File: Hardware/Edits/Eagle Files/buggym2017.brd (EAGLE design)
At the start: 88.9 x 81.3 mm, 6 parts, among them IC1-NOR 4001N, IC2-OR 4075N, IC3 BCC, IC4 L293E

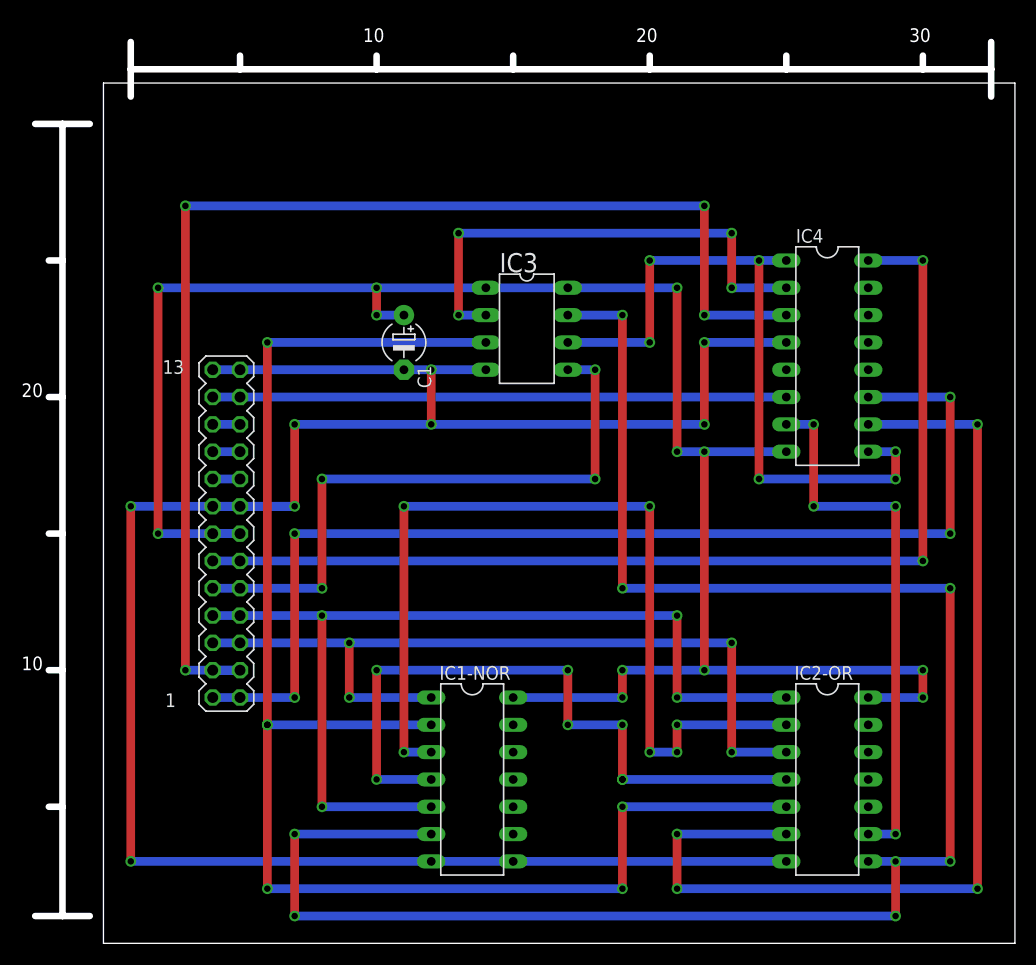
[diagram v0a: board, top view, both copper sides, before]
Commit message: Rerouted ground and the left motor signal Ground went around the header in a column that is not actually present on the board. Fixed Moved 3 pre-placed wires, so that the left motor signal wire does not have to go under the H-bridge. All changes are in diameter 0.016 (thin) red wire
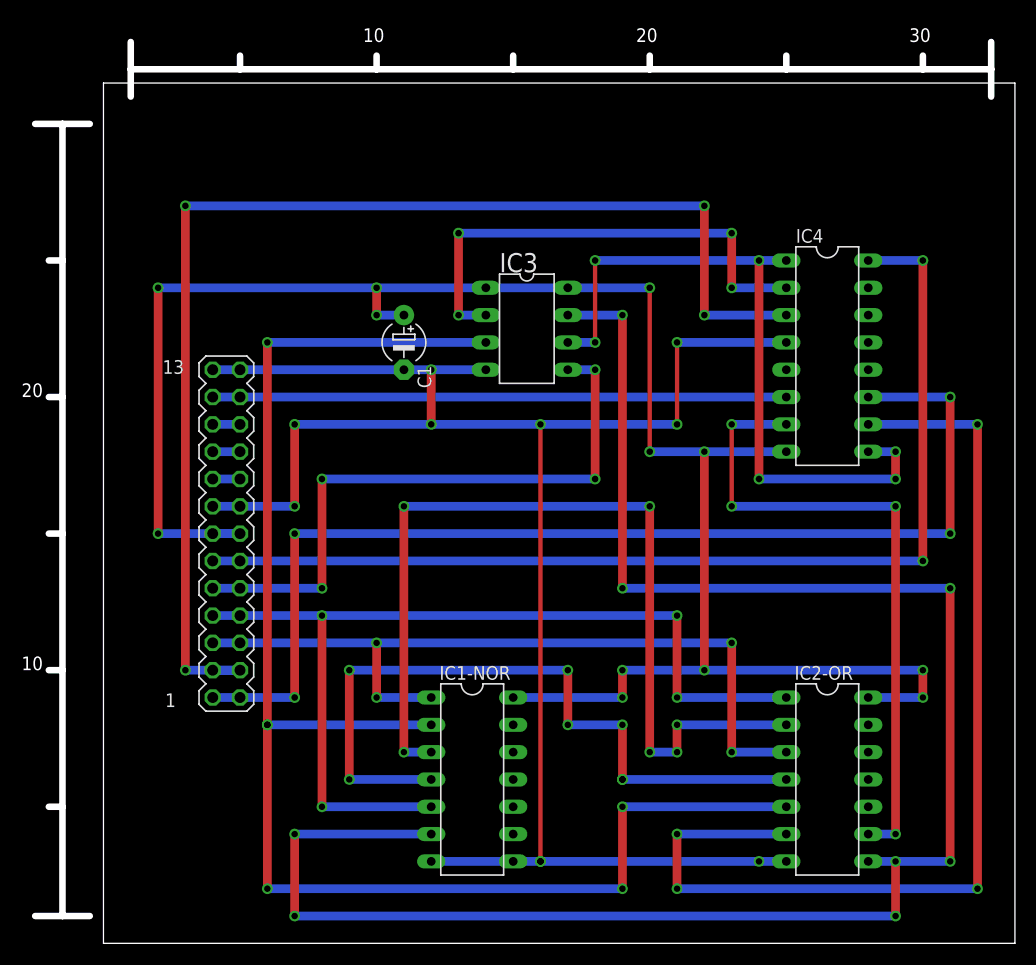
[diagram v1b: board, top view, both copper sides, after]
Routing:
- net GND: track 203.2 -> 167.6 mm, vias 8 -> 10
- net LM: track 50.8 -> 61.0 mm
- net LINK_2: track 63.5 -> 68.6 mm
- net R_EYE: track 73.7 -> 71.1 mm
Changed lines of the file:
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@@
 <?xml version="1.0" encoding="utf-8"?>
 <!DOCTYPE eagle SYSTEM "eagle.dtd">
-<eagle version="7.7.0">
+<eagle version="8.0.1">
 <drawing>
 <settings>
@@
 <text x="65.405" y="42.545" size="1.778" layer="19">X</text>
 <text x="29.845" y="42.545" size="1.778" layer="19">X</text>
-<text x="65.405" y="45.085" size="1.778" layer="19">X</text>
+<text x="62.865" y="45.085" size="1.778" layer="19">X</text>
 <text x="83.185" y="45.085" size="1.778" layer="19">X</text>
 <text x="83.185" y="47.625" size="1.778" layer="19">X</text>
 <text x="83.185" y="50.165" size="1.778" layer="19">X</text>
 <text x="83.185" y="62.865" size="1.778" layer="19">X</text>
-<text x="73.025" y="47.625" size="1.778" layer="19">X</text>
+<text x="70.485" y="47.625" size="1.778" layer="19">X</text>
 <text x="29.845" y="47.625" size="1.778" layer="19">X</text>
 <text x="55.245" y="52.705" size="1.778" layer="19">X</text>
@@
 <text x="55.245" y="57.785" size="1.778" layer="19">X</text>
 <text x="70.485" y="60.325" size="1.778" layer="19">X</text>
-<text x="67.945" y="57.785" size="1.778" layer="19">X</text>
-<text x="67.945" y="55.245" size="1.778" layer="19">X</text>
+<text x="65.405" y="57.785" size="1.778" layer="19">X</text>
+<text x="65.405" y="55.245" size="1.778" layer="19">X</text>
 <text x="45.085" y="57.785" size="1.778" layer="19">X</text>
 <text x="83.185" y="60.325" size="1.778" layer="19">X</text>
 <text x="83.185" y="57.785" size="1.778" layer="19">X</text>
-<text x="67.945" y="52.705" size="1.778" layer="19">X</text>
+<text x="65.405" y="52.705" size="1.778" layer="19">X</text>
 <text x="83.185" y="22.225" size="1.778" layer="19">X</text>
 <text x="83.185" y="19.685" size="1.778" layer="19">X</text>
@@
 <contactref element="IC4" pad="9"/>
 <contactref element="IC4" pad="1"/>
-<wire x1="58.42" y1="55.88" x2="66.04" y2="55.88" width="0.8128" layer="16"/>
-<via x="66.04" y="55.88" extent="1-16" drill="0.6096" shape="square"/>
-<wire x1="66.04" y1="55.88" x2="66.04" y2="63.5" width="0.8128" layer="1"/>
-<via x="66.04" y="63.5" extent="1-16" drill="0.6096" shape="square"/>
-<wire x1="66.04" y1="63.5" x2="76.2" y2="63.5" width="0.8128" layer="16"/>
+<wire x1="58.42" y1="55.88" x2="60.96" y2="55.88" width="0.8128" layer="16"/>
+<via x="60.96" y="55.88" extent="1-16" drill="0.6096" shape="square"/>
+<wire x1="60.96" y1="55.88" x2="60.96" y2="63.5" width="0.4064" layer="1"/>
+<via x="60.96" y="63.5" extent="1-16" drill="0.6096" shape="square"/>
+<wire x1="60.96" y1="63.5" x2="76.2" y2="63.5" width="0.8128" layer="16"/>
 <wire x1="76.2" y1="63.5" x2="78.74" y2="63.5" width="0.8128" layer="16"/>
 <wire x1="86.36" y1="45.72" x2="88.9" y2="45.72" width="0.8128" layer="16"/>
@@
 <wire x1="40.64" y1="58.42" x2="40.64" y2="60.96" width="0.8128" layer="1"/>
 <wire x1="78.74" y1="45.72" x2="71.12" y2="45.72" width="0.8128" layer="16"/>
-<via x="68.58" y="45.72" extent="1-16" drill="0.6096" shape="square"/>
-<wire x1="71.12" y1="45.72" x2="68.58" y2="45.72" width="0.8128" layer="16"/>
-<wire x1="68.58" y1="45.72" x2="68.58" y2="60.96" width="0.8128" layer="1"/>
-<via x="68.58" y="60.96" extent="1-16" drill="0.6096" shape="square"/>
-<wire x1="68.58" y1="60.96" x2="58.42" y2="60.96" width="0.8128" layer="16"/>
+<via x="66.04" y="45.72" extent="1-16" drill="0.6096" shape="square"/>
+<wire x1="71.12" y1="45.72" x2="66.04" y2="45.72" width="0.8128" layer="16"/>
+<wire x1="66.04" y1="45.72" x2="66.04" y2="60.96" width="0.4064" layer="1"/>
+<via x="66.04" y="60.96" extent="1-16" drill="0.6096" shape="square"/>
+<wire x1="66.04" y1="60.96" x2="58.42" y2="60.96" width="0.8128" layer="16"/>
 <via x="40.64" y="60.96" extent="1-16" drill="0.6096" shape="square"/>
 <contactref element="IC1-NOR" pad="14"/>
@@
 <wire x1="43.18" y1="53.34" x2="45.72" y2="53.34" width="0.8128" layer="16"/>
 <wire x1="45.72" y1="53.34" x2="50.8" y2="53.34" width="0.8128" layer="16"/>
-<wire x1="78.74" y1="55.88" x2="71.12" y2="55.88" width="0.8128" layer="16"/>
-<via x="71.12" y="55.88" extent="1-16" drill="0.6096" shape="square"/>
-<wire x1="71.12" y1="55.88" x2="71.12" y2="48.26" width="0.8128" layer="1"/>
-<via x="71.12" y="48.26" extent="1-16" drill="0.6096" shape="square"/>
-<wire x1="71.12" y1="48.26" x2="45.72" y2="48.26" width="0.8128" layer="16"/>
+<wire x1="78.74" y1="55.88" x2="68.58" y2="55.88" width="0.8128" layer="16"/>
+<via x="68.58" y="55.88" extent="1-16" drill="0.6096" shape="square"/>
+<wire x1="68.58" y1="55.88" x2="68.58" y2="48.26" width="0.4064" layer="1"/>
+<via x="68.58" y="48.26" extent="1-16" drill="0.6096" shape="square"/>
+<wire x1="68.58" y1="48.26" x2="55.88" y2="48.26" width="0.8128" layer="16"/>
 <via x="45.72" y="48.26" extent="1-16" drill="0.6096" shape="square"/>
+<wire x1="55.88" y1="48.26" x2="45.72" y2="48.26" width="0.8128" layer="16"/>
 <wire x1="45.72" y1="48.26" x2="45.72" y2="53.34" width="0.8128" layer="1"/>
 <contactref element="BUGGY_CON" pad="8"/>
@@
 <contactref element="IC2-OR" pad="7"/>
 <wire x1="27.94" y1="40.64" x2="33.02" y2="40.64" width="0.8128" layer="16"/>
-<wire x1="33.02" y1="40.64" x2="17.78" y2="40.64" width="0.8128" layer="16"/>
-<via x="17.78" y="40.64" extent="1-16" drill="0.6" shape="square"/>
-<wire x1="17.78" y1="40.64" x2="17.78" y2="7.62" width="0.8128" layer="1"/>
-<via x="17.78" y="7.62" extent="1-16" drill="0.6" shape="square"/>
-<wire x1="17.78" y1="7.62" x2="45.72" y2="7.62" width="0.8128" layer="16"/>
-<wire x1="45.72" y1="7.62" x2="78.74" y2="7.62" width="0.8128" layer="16"/>
+<wire x1="45.72" y1="7.62" x2="55.88" y2="7.62" width="0.8128" layer="16"/>
+<wire x1="55.88" y1="7.62" x2="76.2" y2="7.62" width="0.8128" layer="16"/>
+<wire x1="76.2" y1="7.62" x2="78.74" y2="7.62" width="0.8128" layer="16"/>
+<via x="76.2" y="7.62" extent="1-16" drill="0.6" shape="square"/>
+<via x="55.88" y="7.62" extent="1-16" drill="0.6" shape="square"/>
+<via x="55.88" y="7.62" extent="1-16" drill="0.6" shape="square"/>
+<wire x1="55.88" y1="7.62" x2="55.88" y2="48.26" width="0.4064" layer="1"/>
+<via x="55.88" y="48.26" extent="1-16" drill="0.6" shape="square"/>
 </signal>
 <signal name="N$2">
@@
 <contactref element="BUGGY_CON" pad="3"/>
 <contactref element="IC2-OR" pad="3"/>
-<wire x1="38.1" y1="27.94" x2="27.94" y2="27.94" width="0.8128" layer="16"/>
-<via x="38.1" y="27.94" extent="1-16" drill="0.6" shape="square"/>
-<wire x1="38.1" y1="27.94" x2="38.1" y2="22.86" width="0.8128" layer="1"/>
-<via x="38.1" y="22.86" extent="1-16" drill="0.6" shape="square"/>
-<wire x1="38.1" y1="22.86" x2="45.72" y2="22.86" width="0.8128" layer="16"/>
+<wire x1="40.64" y1="27.94" x2="27.94" y2="27.94" width="0.8128" layer="16"/>
+<via x="40.64" y="27.94" extent="1-16" drill="0.6" shape="square"/>
+<wire x1="40.64" y1="27.94" x2="40.64" y2="22.86" width="0.8128" layer="1"/>
+<via x="40.64" y="22.86" extent="1-16" drill="0.6" shape="square"/>
+<wire x1="40.64" y1="22.86" x2="45.72" y2="22.86" width="0.8128" layer="16"/>
 <wire x1="78.74" y1="17.78" x2="73.66" y2="17.78" width="0.8128" layer="16"/>
 <via x="73.66" y="17.78" extent="1-16" drill="0.6" shape="square"/>
 <wire x1="73.66" y1="17.78" x2="73.66" y2="27.94" width="0.8128" layer="1"/>
 <via x="73.66" y="27.94" extent="1-16" drill="0.6" shape="square"/>
-<wire x1="73.66" y1="27.94" x2="38.1" y2="27.94" width="0.8128" layer="16"/>
+<wire x1="73.66" y1="27.94" x2="40.64" y2="27.94" width="0.8128" layer="16"/>
 </signal>
 <signal name="L_EYE">
@@
 <contactref element="IC1-NOR" pad="4"/>
 <contactref element="IC2-OR" pad="4"/>
-<wire x1="45.72" y1="15.24" x2="40.64" y2="15.24" width="0.8128" layer="16"/>
-<via x="40.64" y="15.24" extent="1-16" drill="0.6" shape="square"/>
-<wire x1="40.64" y1="15.24" x2="40.64" y2="25.4" width="0.8128" layer="1"/>
-<via x="40.64" y="25.4" extent="1-16" drill="0.6" shape="square"/>
-<wire x1="40.64" y1="25.4" x2="58.42" y2="25.4" width="0.8128" layer="16"/>
+<wire x1="45.72" y1="15.24" x2="38.1" y2="15.24" width="0.8128" layer="16"/>
+<via x="38.1" y="15.24" extent="1-16" drill="0.6" shape="square"/>
+<wire x1="38.1" y1="15.24" x2="38.1" y2="25.4" width="0.8128" layer="1"/>
+<via x="38.1" y="25.4" extent="1-16" drill="0.6" shape="square"/>
+<wire x1="38.1" y1="25.4" x2="58.42" y2="25.4" width="0.8128" layer="16"/>
 <via x="58.42" y="25.4" extent="1-16" drill="0.6" shape="square"/>
 <wire x1="58.42" y1="25.4" x2="58.42" y2="20.32" width="0.8128" layer="1"/>
@@
 <wire x1="88.9" y1="10.16" x2="88.9" y2="40.64" width="0.8128" layer="1"/>
 <via x="88.9" y="40.64" extent="1-16" drill="0.6" shape="square"/>
-<wire x1="88.9" y1="40.64" x2="81.28" y2="40.64" width="0.8128" layer="16"/>
-<via x="81.28" y="40.64" extent="1-16" drill="0.6" shape="square"/>
-<wire x1="81.28" y1="40.64" x2="81.28" y2="48.26" width="0.8128" layer="1"/>
-<via x="81.28" y="48.26" extent="1-16" drill="0.6" shape="square"/>
-<wire x1="81.28" y1="48.26" x2="78.74" y2="48.26" width="0.8128" layer="16"/>
+<wire x1="88.9" y1="40.64" x2="73.66" y2="40.64" width="0.8128" layer="16"/>
+<via x="73.66" y="40.64" extent="1-16" drill="0.6" shape="square"/>
+<wire x1="73.66" y1="40.64" x2="73.66" y2="48.26" width="0.4064" layer="1"/>
+<via x="73.66" y="48.26" extent="1-16" drill="0.6" shape="square"/>
+<wire x1="73.66" y1="48.26" x2="78.74" y2="48.26" width="0.8128" layer="16"/>
 </signal>
 <signal name="RM">

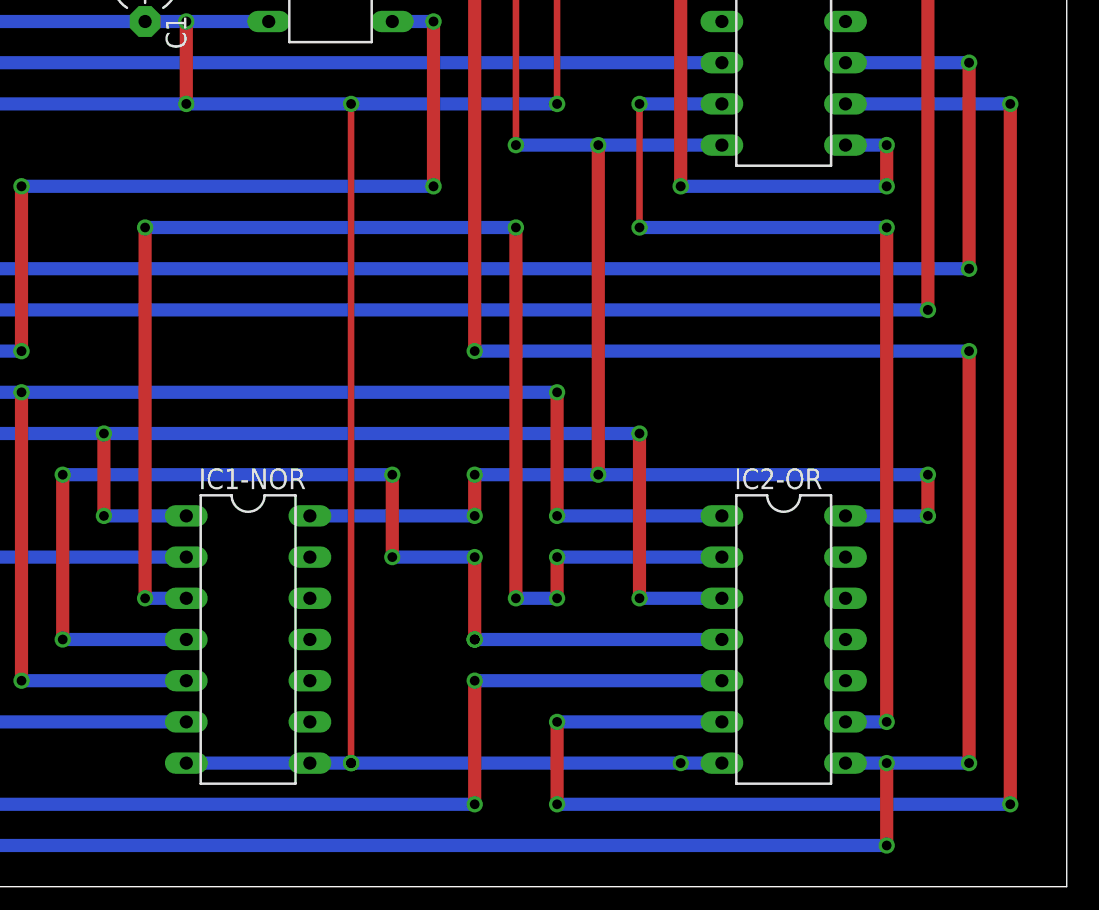
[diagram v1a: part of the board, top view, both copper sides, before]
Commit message: Work done in Hardware Lab 5
Finished schematic and new Arduino Sketch, blink without delay
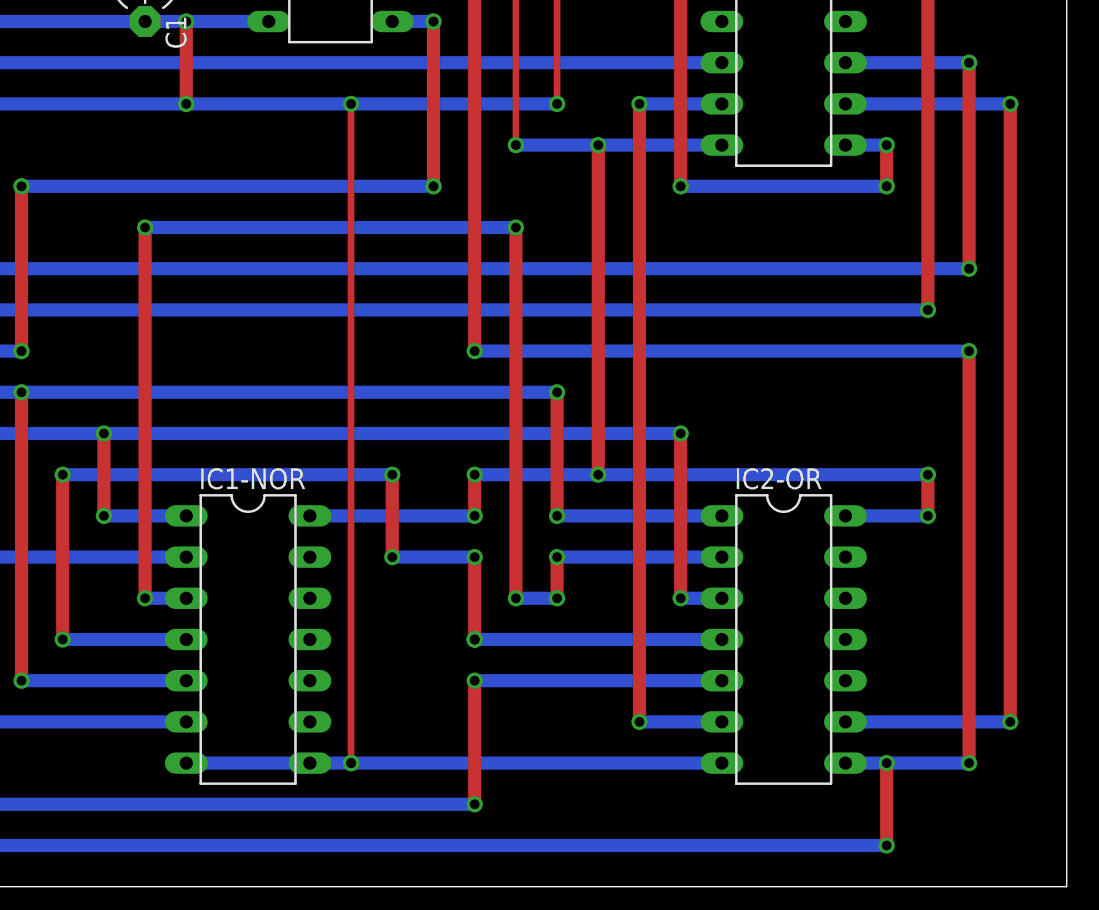
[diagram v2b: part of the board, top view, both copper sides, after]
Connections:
- net LM: now also IC4.10; no longer IC4.7
- net RM: now also IC4.7; no longer IC4.10
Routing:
- net RM: track 96.5 -> 48.3 mm, vias 4 -> 2
- net LM: track 61.0 -> 58.4 mm, vias 4 -> 2
- net GND: vias 10 -> 9
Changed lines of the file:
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@@
 <?xml version="1.0" encoding="utf-8"?>
 <!DOCTYPE eagle SYSTEM "eagle.dtd">
-<eagle version="8.0.1">
+<eagle version="7.7.0">
 <drawing>
 <settings>
@@
 <wire x1="27.94" y1="40.64" x2="33.02" y2="40.64" width="0.8128" layer="16"/>
 <wire x1="45.72" y1="7.62" x2="55.88" y2="7.62" width="0.8128" layer="16"/>
-<wire x1="55.88" y1="7.62" x2="76.2" y2="7.62" width="0.8128" layer="16"/>
-<wire x1="76.2" y1="7.62" x2="78.74" y2="7.62" width="0.8128" layer="16"/>
-<via x="76.2" y="7.62" extent="1-16" drill="0.6" shape="square"/>
 <via x="55.88" y="7.62" extent="1-16" drill="0.6" shape="square"/>
 <via x="55.88" y="7.62" extent="1-16" drill="0.6" shape="square"/>
 <wire x1="55.88" y1="7.62" x2="55.88" y2="48.26" width="0.4064" layer="1"/>
 <via x="55.88" y="48.26" extent="1-16" drill="0.6" shape="square"/>
+<wire x1="55.88" y1="7.62" x2="78.74" y2="7.62" width="0.8128" layer="16"/>
 </signal>
 <signal name="N$2">
@@
 <via x="40.64" y="22.86" extent="1-16" drill="0.6" shape="square"/>
 <wire x1="40.64" y1="22.86" x2="45.72" y2="22.86" width="0.8128" layer="16"/>
-<wire x1="78.74" y1="17.78" x2="73.66" y2="17.78" width="0.8128" layer="16"/>
-<via x="73.66" y="17.78" extent="1-16" drill="0.6" shape="square"/>
-<wire x1="73.66" y1="17.78" x2="73.66" y2="27.94" width="0.8128" layer="1"/>
-<via x="73.66" y="27.94" extent="1-16" drill="0.6" shape="square"/>
-<wire x1="73.66" y1="27.94" x2="40.64" y2="27.94" width="0.8128" layer="16"/>
+<wire x1="78.74" y1="17.78" x2="76.2" y2="17.78" width="0.8128" layer="16"/>
+<via x="76.2" y="17.78" extent="1-16" drill="0.6" shape="square"/>
+<wire x1="76.2" y1="17.78" x2="76.2" y2="27.94" width="0.8128" layer="1"/>
+<via x="76.2" y="27.94" extent="1-16" drill="0.6" shape="square"/>
+<wire x1="76.2" y1="27.94" x2="40.64" y2="27.94" width="0.8128" layer="16"/>
 </signal>
 <signal name="L_EYE">
@@
 <signal name="LM">
 <contactref element="IC2-OR" pad="9"/>
+<contactref element="IC4" pad="10"/>
+<wire x1="86.36" y1="10.16" x2="96.52" y2="10.16" width="0.8128" layer="16"/>
+<via x="96.52" y="10.16" extent="1-16" drill="0.6" shape="square"/>
+<wire x1="96.52" y1="10.16" x2="96.52" y2="48.26" width="0.8128" layer="1"/>
+<via x="96.52" y="48.26" extent="1-16" drill="0.6" shape="square"/>
+<wire x1="96.52" y1="48.26" x2="86.36" y2="48.26" width="0.8128" layer="16"/>
+</signal>
+<signal name="RM">
+<contactref element="IC2-OR" pad="6"/>
 <contactref element="IC4" pad="7"/>
-<wire x1="86.36" y1="10.16" x2="88.9" y2="10.16" width="0.8128" layer="16"/>
-<via x="88.9" y="10.16" extent="1-16" drill="0.6" shape="square"/>
-<wire x1="88.9" y1="10.16" x2="88.9" y2="40.64" width="0.8128" layer="1"/>
-<via x="88.9" y="40.64" extent="1-16" drill="0.6" shape="square"/>
-<wire x1="88.9" y1="40.64" x2="73.66" y2="40.64" width="0.8128" layer="16"/>
-<via x="73.66" y="40.64" extent="1-16" drill="0.6" shape="square"/>
-<wire x1="73.66" y1="40.64" x2="73.66" y2="48.26" width="0.4064" layer="1"/>
+<wire x1="78.74" y1="10.16" x2="73.66" y2="10.16" width="0.8128" layer="16"/>
+<via x="73.66" y="10.16" extent="1-16" drill="0.6" shape="square"/>
+<wire x1="73.66" y1="10.16" x2="73.66" y2="48.26" width="0.8128" layer="1"/>
 <via x="73.66" y="48.26" extent="1-16" drill="0.6" shape="square"/>
 <wire x1="73.66" y1="48.26" x2="78.74" y2="48.26" width="0.8128" layer="16"/>
 </signal>
-<signal name="RM">
-<contactref element="IC2-OR" pad="6"/>
-<contactref element="IC4" pad="10"/>
-<wire x1="78.74" y1="10.16" x2="68.58" y2="10.16" width="0.8128" layer="16"/>
-<via x="68.58" y="10.16" extent="1-16" drill="0.6" shape="square"/>
-<wire x1="68.58" y1="10.16" x2="68.58" y2="5.08" width="0.8128" layer="1"/>
-<via x="68.58" y="5.08" extent="1-16" drill="0.6" shape="square"/>
-<wire x1="68.58" y1="5.08" x2="96.52" y2="5.08" width="0.8128" layer="16"/>
-<via x="96.52" y="5.08" extent="1-16" drill="0.6" shape="square"/>
-<wire x1="96.52" y1="5.08" x2="96.52" y2="48.26" width="0.8128" layer="1"/>
-<via x="96.52" y="48.26" extent="1-16" drill="0.6" shape="square"/>
-<wire x1="96.52" y1="48.26" x2="86.36" y2="48.26" width="0.8128" layer="16"/>
-</signal>
 <signal name="N$1">
